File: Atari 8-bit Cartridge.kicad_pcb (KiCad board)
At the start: 2 copper layers, 54.6 x 59.3 mm, 13 parts, among them J2 Atari 8-bit Left Cartridge Co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, U0 27C128, U1 27C64, U2 74AHCT1G08

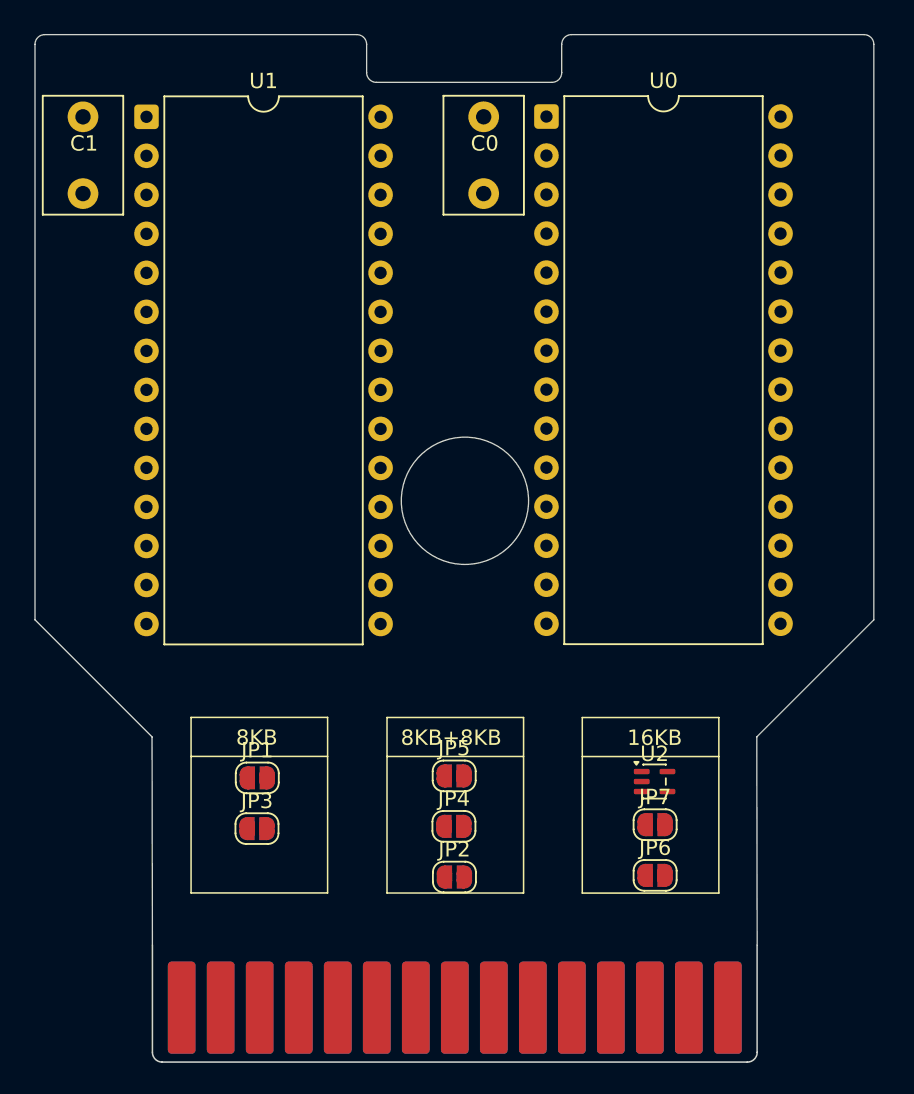
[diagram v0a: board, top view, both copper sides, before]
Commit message: Lay out configuration jumpers.
This required moving quite a bit around to make room.
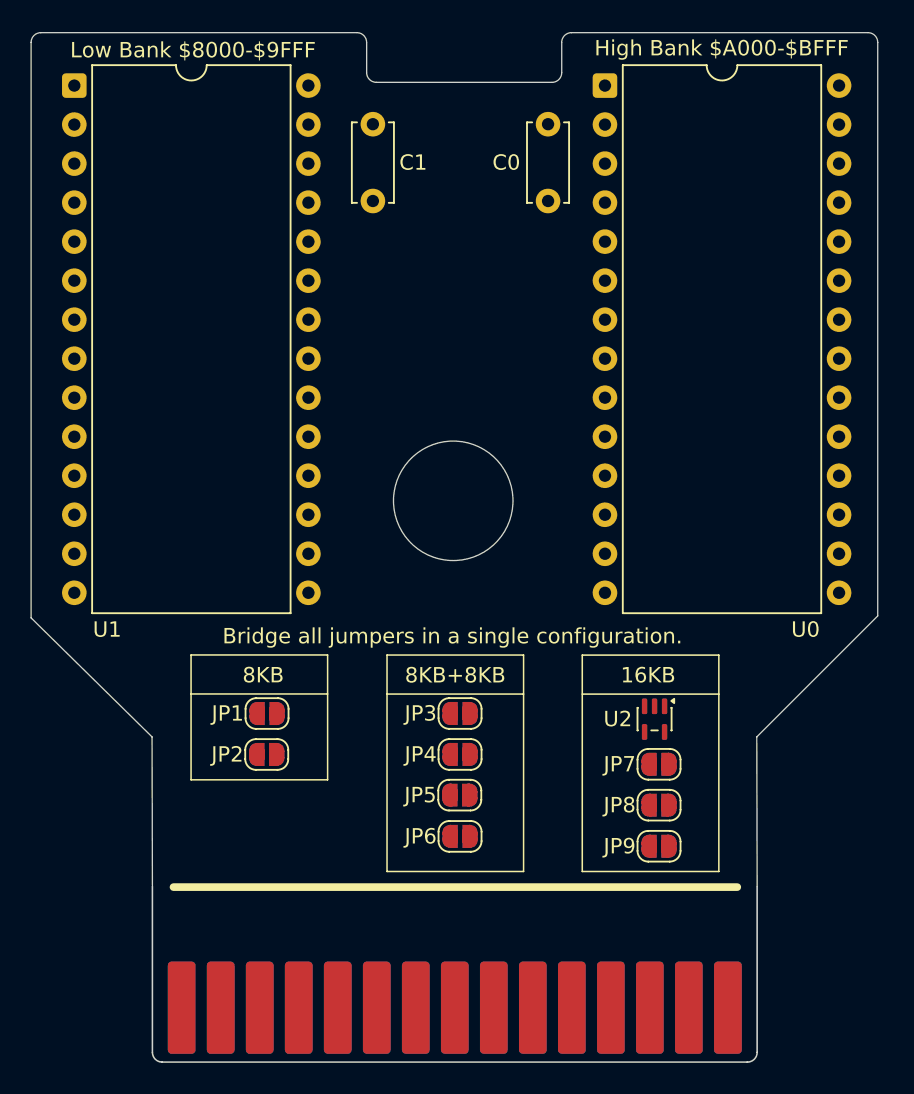
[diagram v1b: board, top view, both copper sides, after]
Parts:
- removed the JP6 at (120.4, 111.9)
- added JP4: High_Bank_Present_8+8KB, Atari_8-bit:SolderJumper, F.Cu at (107.7, 104.0)
- added JP7: Low_Bank_Present_16KB, Atari_8-bit:SolderJumper, F.Cu at (120.6, 104.7)
- added JP8: High_Bank_Present_16KB, Atari_8-bit:SolderJumper, F.Cu at (120.6, 107.3)
- C0, C1: value C -> 100nF; footprint Capacitor_THT:C_Disc_D7.5mm_W5.0mm_P5.00mm -> Capacitor_THT:C_Disc_D5.0mm_W2.5mm_P5.00mm
- JP1: value High_Bank_Present -> High_Bank_Present_8KB; footprint Jumper:SolderJumper-2_P1.3mm_Open_RoundedPad1.0x1.5mm -> Atari_8-bit:SolderJumper
- JP2: renamed from JP3; footprint Jumper:SolderJumper-2_P1.3mm_Open_RoundedPad1.0x1.5mm -> Atari_8-bit:SolderJumper
- JP3: renamed from JP2; value High+Low_Bank_Present -> Low_Bank_Present_8+8KB; footprint Jumper:SolderJumper-2_P1.3mm_Open_RoundedPad1.0x1.5mm -> Atari_8-bit:SolderJumper
- JP5: renamed from JP4; footprint Jumper:SolderJumper-2_P1.3mm_Open_RoundedPad1.0x1.5mm -> Atari_8-bit:SolderJumper
- JP6: renamed from JP5; footprint Jumper:SolderJumper-2_P1.3mm_Open_RoundedPad1.0x1.5mm -> Atari_8-bit:SolderJumper
- JP9: renamed from JP7; footprint Jumper:SolderJumper-2_P1.3mm_Open_RoundedPad1.0x1.5mm -> Atari_8-bit:SolderJumper
- moved C1 18.9 mm to (102.0, 63.0)
- moved JP3 10.7 mm to (107.7, 101.3)
- moved U1 5.12 mm to (82.6, 60.5)
- moved JP2 4.87 mm to (95.1, 104.0)
- moved U0 4.31 mm to (117.1, 60.5)
- moved JP1 4.24 mm to (95.1, 101.3)
- moved C0 4.22 mm to (113.4, 63.0)
- moved U2 4.06 mm to (120.3, 101.7), turned to -90 degrees
- moved JP6 3.96 mm to (107.7, 109.3)
- moved JP5 2.07 mm to (107.7, 106.7)
- moved JP9 1.43 mm to (120.6, 110.0)
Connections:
- J2 pad 14: /RD4 -> /RD5
- JP1 pad 2: /RD4 -> /RD5
- U0 pad 26: /U1_Enable -> //S4
- U2 pad 1: //S4 -> unconnected-(U2-Pad1)
- U2 pad 2: //S5 -> unconnected-(U2-Pad2)
- U2 pad 4: /U0_Enable_16KB -> unconnected-(U2-Pad4)
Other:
- board size 54.6 x 59.3 mm -> 55.1 x 55.6 mm
- board text added: "Bridge all jumpers in a single configuration."
- board text added: "High Bank $A000-$BFFF"
- board text added: "Low Bank $8000-$9FFF"

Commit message: Remove soldermask from edge connector.
It can wear off and gunk up the cartridge slot.
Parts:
- renumbered J2 to J1
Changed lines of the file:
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@@
 		(layer "F.Cu")
 		(at 87.654 121.5)
-		(property "Reference" "J2"
+		(property "Reference" "J1"
 			(at 5 -3.5 0)
 			(layer "F.SilkS")
@@
 		(sheetname "/")
 		(sheetfile "Atari 8-bit Cartridge.kicad_sch")
-		(units
-			(unit
-				(name "A")
-				(pins "1" "2" "3" "4" "5" "6" "7" "8" "9" "10" "11" "12" "13" "14" "15"
-					"A" "B" "C" "D" "E" "F" "H" "J" "K" "L" "M" "N" "P" "R" "S"
-				)
-			)
-		)
 		(duplicate_pad_numbers_are_jumpers no)
+		(fp_rect
+			(start 0 -4.445)
+			(end 39.37 2.54)
+			(stroke
+				(width 0.1)
+				(type solid)
+			)
+			(fill yes)
+			(layer "F.Mask")
+		)
+		(fp_rect
+			(start 0 -4.445)
+			(end 39.37 2.54)
+			(stroke
+				(width 0.1)
+				(type solid)
+			)
+			(fill yes)
+			(layer "B.Mask")
+		)
 		(fp_line
 			(start 0 -8.89)
@@
 		(fp_line
 			(start 39.37 2.54)
-			(end 39.37 -5.08)
+			(end 39.37 -8.89)
 			(stroke
 				(width 0.05)
@@
 			(layers "F.Cu" "F.Mask")
 			(roundrect_rratio 0.1388888889)
-			(net "unconnected-(J2-{slash}CCTL-Pad15)")
+			(net "unconnected-(J1-{slash}CCTL-Pad15)")
 			(pinfunction "/CCTL_15")
 			(pintype "output+no_connect")
@@
 			(layers "B.Cu" "B.Mask")
 			(roundrect_rratio 0.1388888889)
-			(net "unconnected-(J2-R{slash}W-PadR)")
+			(net "unconnected-(J1-R{slash}W-PadR)")
 			(pinfunction "R/W_R")
 			(pintype "output+no_connect")
@@
 			(layers "B.Cu" "B.Mask")
 			(roundrect_rratio 0.1388888889)
-			(net "unconnected-(J2-B-PHI2-PadS)")
+			(net "unconnected-(J1-B-PHI2-PadS)")
 			(pinfunction "B-PHI2_S")
 			(pintype "output+no_connect")

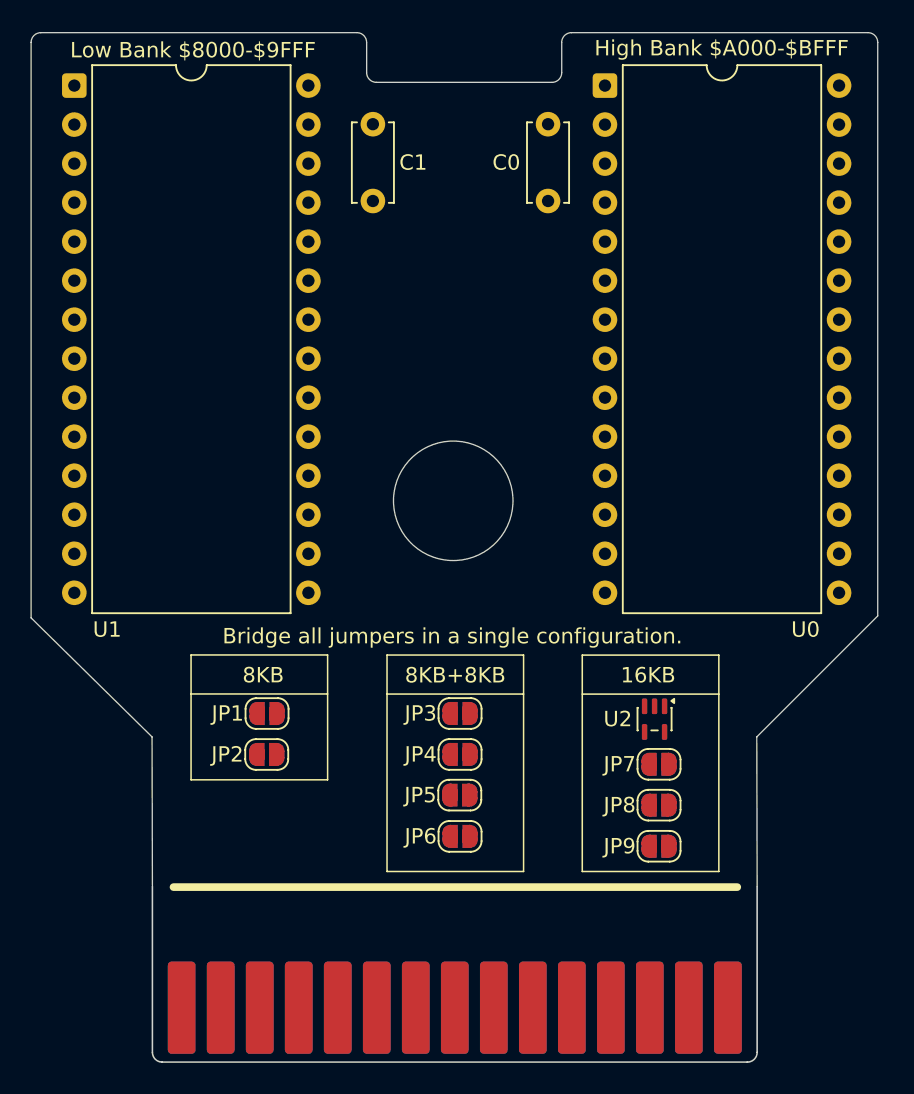
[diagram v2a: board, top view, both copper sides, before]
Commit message: First routing pass of back copper.
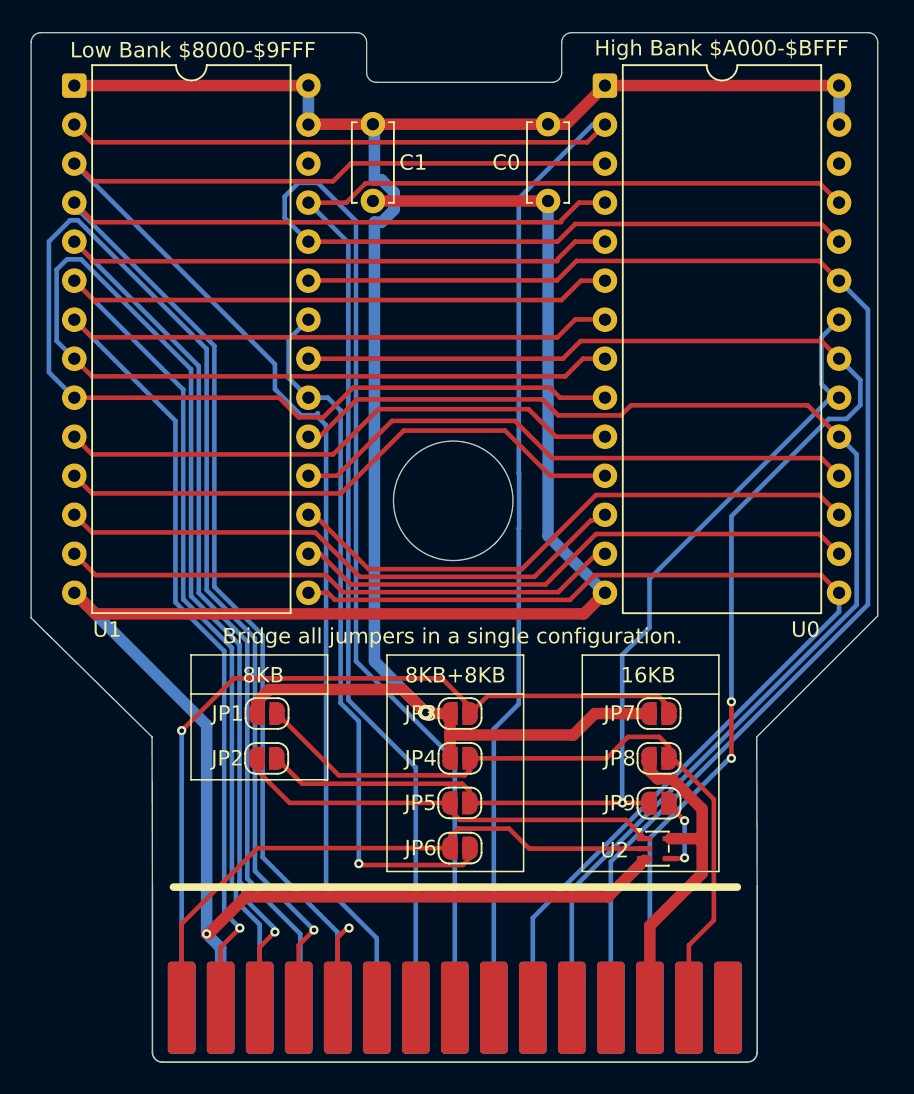
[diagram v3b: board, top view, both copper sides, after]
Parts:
- moved U2 8.43 mm to (120.5, 110.1), turned to 0 degrees
- moved JP7 3.30 mm to (120.6, 101.4)
- moved JP8 3.05 mm to (120.6, 104.3)
- moved JP9 2.80 mm to (120.6, 107.2)
- moved JP6 0.76 mm to (107.7, 110.1)
- moved JP5 0.51 mm to (107.7, 107.2)
- moved JP2 0.25 mm to (95.1, 104.3)
- moved JP4 0.25 mm to (107.7, 104.3)
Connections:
- U2 pad 1: unconnected-(U2-Pad1) -> //S5
- U2 pad 2: unconnected-(U2-Pad2) -> //S4
- U2 pad 4: unconnected-(U2-Pad4) -> /U0_Enable_16KB
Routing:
- net +5V: track 0.00 -> 149.8 mm, vias 0 -> 1
- net GND: track 0.00 -> 135.6 mm, vias 0 -> 1
- net /A1: track 0.00 -> 107.5 mm, vias 0 -> 1
- net /A7: track 0.00 -> 99.5 mm
- net /A9: track 0.00 -> 99.0 mm
- net /A2: track 0.00 -> 98.0 mm, vias 0 -> 1
- net /A12: track 0.00 -> 96.5 mm
- net /A6: track 0.00 -> 95.3 mm
- net /A5: track 0.00 -> 91.5 mm
- net /A8: track 0.00 -> 90.9 mm
- net /A11: track 0.00 -> 90.7 mm
- net /A4: track 0.00 -> 88.0 mm
- net /A3: track 0.00 -> 85.3 mm, vias 0 -> 1
- net /A10: track 0.00 -> 84.9 mm, vias 0 -> 2
- net /D7: track 0.00 -> 82.4 mm
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
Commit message: Finish routing front and back copper.
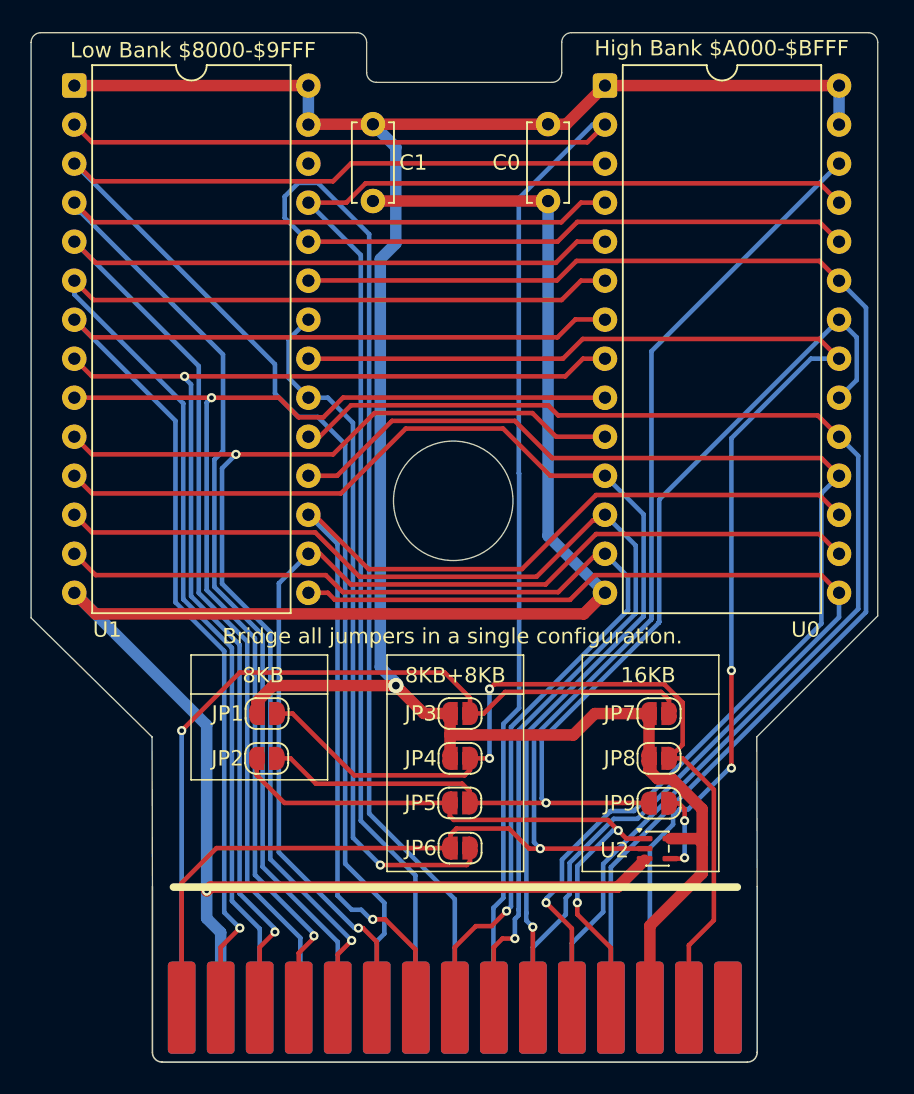
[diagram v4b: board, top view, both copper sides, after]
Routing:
- net //S4: track 39.1 -> 93.8 mm, vias 0 -> 1
- net /D6: track 37.5 -> 81.6 mm, vias 0 -> 1
- net /D0: track 37.9 -> 77.1 mm, vias 0 -> 1
- net /D1: track 37.9 -> 75.1 mm, vias 0 -> 1
- net /D5: track 38.5 -> 74.4 mm, vias 0 -> 1
- net /D2: track 36.6 -> 72.1 mm, vias 0 -> 1
- net /A0: track 42.6 -> 77.0 mm, vias 1 -> 2
- net /D4: track 37.3 -> 70.6 mm, vias 0 -> 1
- net /A1: track 107.5 -> 78.9 mm, vias 1 -> 2
- net /A2: track 98.0 -> 79.4 mm, vias 1 -> 2
- net //S5: track 28.1 -> 42.3 mm, vias 0 -> 2
- net /RD5: track 48.1 -> 56.9 mm, vias 0 -> 2
- net /U0_Enable: track 64.6 -> 72.1 mm
- net GND: track 135.6 -> 134.4 mm
- net /D3: track 71.2 -> 72.1 mm
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
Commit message: Add ground fills and via stitching.
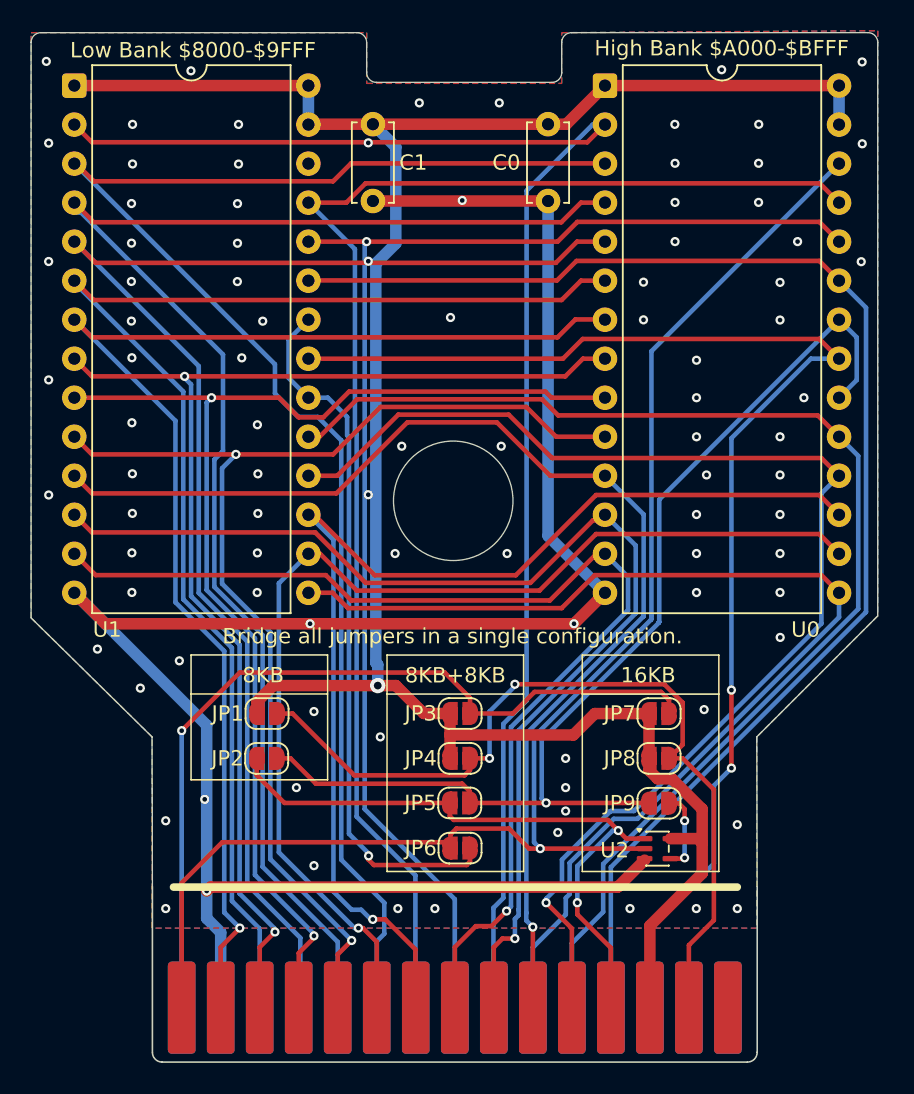
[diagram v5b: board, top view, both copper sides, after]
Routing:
- net /A9: track 99.1 -> 88.0 mm, vias 0 -> 1
- net /RD5: track 56.9 -> 56.1 mm
- net /A10: track 84.6 -> 84.0 mm
- net GND: track 134.4 -> 135.0 mm, vias 1 -> 95
- added copper zone on B.Cu, net GND
- added copper zone on F.Cu, net GND
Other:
- board text added: "Atari 8-Bit (400/800/XL/XE) Cartridge V1.0 Sean D. Cline https://sdcline.com/atari8bitcart"
